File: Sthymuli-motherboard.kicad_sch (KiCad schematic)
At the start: 270 parts, among them J1 USB_C_Receptacle_USB2.0_16P, J2 Conn_01x09, J3 Conn_01x03, J4 Conn_01x06, Q1 Q_NMOS_Depletion_GSD, Q10 NX7002AK, Q11 NX7002AK, Q12 NX7002AK, Q13 NX7002AK, Q14 NX7002AK, Q15 NX7002AK, Q2 Q_NMOS_Depletion_GSD, Q3 Q_NMOS_Depletion_GSD, Q4 Q_NMOS_Depletion_GSD, Q5 Q_NMOS_Depletion_GSD, Q6 Q_NMOS_Depletion_GSD, Q7 PMOS, Q8 NX7002AK, Q9 NX7002AK, SW1 SW_Push, SW10 SW_Push, SW2 SW_Push, SW3 SW_Push, SW4 SW_Push, SW5 SW_Push, SW6 SW_Push, SW7 SW_Push, SW8 SW_Push, SW9 SW_Push, U1 ESP32-S3-WROOM-1, U10 74HC4051, U11 MCP6L01x-xOT, U12 74HC4051, U13 LSM6DS3, U14 LSM6DS3, U15 ITR9909, U16 ITR9909, U17 ITR9909, U18 ITR9909, U19 ITR9909, U2 AP2112K-3.3, U20 ITR9909, U21 ITR9909, U22 ITR9909, U3 BQ76905RGRR, U4 AP62300WU, U5 BQ25713, U6 AP62300WU, U7 MCP23017_SO, U8 AP22913CN4, U9 IRM-H6xxT

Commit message: progress on layout
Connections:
- net GND: no longer C80.2, C82.2, C83.2, R49.1
- net GNDA: now also C80.2, C82.2, C83.2, R49.1
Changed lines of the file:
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@@
 	)
 	(symbol
+		(lib_id "power:GNDA")
+		(at 360.68 88.9 0)
+		(unit 1)
+		(exclude_from_sim no)
+		(in_bom yes)
+		(on_board yes)
+		(dnp no)
+		(property "Reference" "#PWR082"
+			(at 360.68 95.25 0)
+			(effects
+				(font
+					(size 1.27 1.27)
+				)
+				(hide yes)
+			)
+		)
+		(property "Value" "GNDA"
+			(at 364.49 88.9 0)
+			(effects
+				(font
+					(size 1.27 1.27)
+				)
+			)
+		)
+		(property "Footprint" ""
+			(at 360.68 88.9 0)
+			(effects
+				(font
+					(size 1.27 1.27)
+				)
+				(hide yes)
+			)
+		)
+		(property "Datasheet" ""
+			(at 360.68 88.9 0)
+			(effects
+				(font
+					(size 1.27 1.27)
+				)
+				(hide yes)
+			)
+		)
+		(property "Description" "Power symbol creates a global label with name \"GNDA\" , analog ground"
+			(at 360.68 88.9 0)
+			(effects
+				(font
+					(size 1.27 1.27)
+				)
+				(hide yes)
+			)
+		)
+		(pin "1"
+		)
+		(instances
+			(project "Sthymuli-motherboard"
+				(path "/a56c3281-40b7-4048-95ca-500415dc80a4"
+					(reference "#PWR082")
+					(unit 1)
+				)
+			)
+		)
+	)
+	(symbol
 		(lib_id "Connector_Generic:Conn_01x03")
 		(at 231.14 374.65 0)
@@
 					(unit 1)
 				)
-			)
-		)
-	)
-	(symbol
-		(lib_id "power:GND")
-		(at 360.68 88.9 0)
-		(mirror y)
-		(unit 1)
-		(exclude_from_sim no)
-		(in_bom yes)
-		(on_board yes)
-		(dnp no)
-		(property "Reference" "#PWR082"
-			(at 360.68 95.25 0)
-			(effects
-				(font
-					(size 1.27 1.27)
-				)
-				(hide yes)
-			)
-		)
-		(property "Value" "GND"
-			(at 358.394 88.9 0)
-			(effects
-				(font
-					(size 1.27 1.27)
-				)
-			)
-		)
-		(property "Footprint" ""
-			(at 360.68 88.9 0)
-			(effects
-				(font
-					(size 1.27 1.27)
-				)
-				(hide yes)
-			)
-		)
-		(property "Datasheet" ""
-			(at 360.68 88.9 0)
-			(effects
-				(font
-					(size 1.27 1.27)
-				)
-				(hide yes)
-			)
-		)
-		(property "Description" "Power symbol creates a global label with name \"GND\" , ground"
-			(at 360.68 88.9 0)
-			(effects
-				(font
-					(size 1.27 1.27)
-				)
-				(hide yes)
-			)
-		)
-		(pin "1"
-		)
-		(instances
-			(project "Sthymuli-motherboard"
-				(path "/a56c3281-40b7-4048-95ca-500415dc80a4"
-					(reference "#PWR082")
-					(unit 1)
-				)

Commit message: starting from scratch the routing. autorouter was not good
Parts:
- removed BT1, BT2, BT3: Battery_Cell, sthymuli:Battery_Holder_18650_robop, symbol Device:Battery_Cell
- removed C10, C11, C12, C13, C14, C15, C16, C17, C18, C19, C20, C21, C22, C23, C24, C25, C77, C8, C9: 100nF, Capacitor_SMD:C_0402_1005Metric, symbol Device:C
- removed D10, D11, D12, D13, D14, D15, D16, D17, D18, D19, D20, D21, D22, D23, D24, D25, D8, D9: WS2812B, LED_SMD:LED_WS2812B_PLCC4_5.0x5.0mm_P3.2mm, symbol LED:WS2812B
- removed D26, D27, D28: D_Schottky, Diode_SMD:D_SOD-123F, symbol Device:D_Schottky
- removed F1, F2, F3: Fuse, Resistor_SMD:R_0805_2012Metric, symbol Device:Fuse
- removed Q10, Q11, Q12, Q13, Q14, Q15: NX7002AK, Package_TO_SOT_SMD:SOT-23, symbol Transistor_FET_Other:Q_NMOS_Depletion_GSD
- removed R52, R53, R54, R55, R56, R57: 3K3, Capacitor_SMD:C_0201_0603Metric, symbol Device:R
- removed R62, R63, R64, R65, R66, R67: 27R, Capacitor_SMD:C_0201_0603Metric, symbol Device:R
- removed SW10, SW5, SW6, SW7, SW8, SW9: SW_Push, sthymuli:XKB5858, symbol Switch:SW_Push
- removed U13: LSM6DS3, Package_LGA:LGA-14_3x2.5mm_P0.5mm_LayoutBorder3x4y, symbol Sensor_Motion:LSM6DS3
- removed U17, U18: ITR9909, sthymuli:ITR_9909_Horizontal, symbol kitprisme:ITR9909
- removed U19, U20, U21, U22: ITR9909, sthymuli:ITR_9909_Vertical, symbol kitprisme:ITR9909
- added J11, J12, J8: Conn_02x08_Counter_Clockwise, Connector_PinSocket_2.54mm:PinSocket_2x08_P2.54mm_Vertical_SMD, symbol Connector_Generic:Conn_02x08_Counter_Clockwise
- J2: footprint Connector_PinHeader_2.54mm:PinHeader_1x09_P2.54mm_Vertical -> Connector_PinSocket_2.54mm:PinSocket_1x09_P2.54mm_Vertical_SMD_Pin1Left
- J3: footprint Connector_PinHeader_2.54mm:PinHeader_1x03_P2.54mm_Vertical -> Connector_PinSocket_2.54mm:PinSocket_1x03_P2.54mm_Vertical_SMD_Pin1Left
- U3: footprint Package_DFN_QFN:Texas_RGP0020H_VQFN-20-1EP_4x4mm_P0.5mm_EP2.4x2.4mm -> BQ76905RGRR:IC_BQ76905RGRR
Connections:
- net +3V3: now also J11.2 (Pin_2), J12.2 (Pin_2), J8.2 (Pin_2)
- net +5V: now also J11.1 (Pin_1), J12.1 (Pin_1), J8.1 (Pin_1)
- net +BATT: now also J11.6 (Pin_6)
- net ACC_B_INT1: now also J12.16 (Pin_16)
- net GND: now also J1.SH (SHIELD), J11.3 (Pin_3), J12.3 (Pin_3), J8.3 (Pin_3); no longer J1.S1 (SHIELD)
- net SCL: now also J11.15 (Pin_15), J12.15 (Pin_15), J8.15 (Pin_15)
- net SDA: now also J11.14 (Pin_14), J12.14 (Pin_14), J8.14 (Pin_14)
- net EAST_BAT+: now reaches R3.1
- net EAST_BAT+: now also J12.7 (Pin_7), J8.6 (Pin_6)
- net at D7.2 (DOUT): now also J8.8 (Pin_8)
- net NORTH_BAT-: now reaches BT4.2 (-), D29.2 (A), R13.2, R14.2, R6.1
- net SOUTH_BAT+: now reaches R2.1
- net SOUTH_BAT+: now also J11.7 (Pin_7), J12.6 (Pin_6)
- net EAST_BAT-: now reaches D29.1 (K), F4.1, R4.1
- net EAST_BAT-: now also J8.7 (Pin_7)
- net INT_WS2812_DIN renamed WS2812_DIN
- net IR_REC_0 renamed NORTH_IR_REC_HORI
- net NORTH_IR_REC_HORI: now also U10.14 (A1); no longer U10.13 (A0)
- net IR_REC_1 renamed NORTH_IR_REC_VERT
- net NORTH_IR_REC_VERT: now also U10.13 (A0); no longer U10.14 (A1)
- net IR_REC_2 renamed EAST_IR_REC_VERT
- net EAST_IR_REC_VERT: now also J8.12 (Pin_12)
- net IR_REC_3 renamed EAST_IR_REC_HORI
- net EAST_IR_REC_HORI: now also J8.10 (Pin_10)
- net IR_REC_4 renamed SOUTH_IR_REC_VERT
- net SOUTH_IR_REC_VERT: now also J12.12 (Pin_12)
- net IR_REC_5 renamed SOUTH_IR_REC_HORI
- net SOUTH_IR_REC_HORI: now also J12.10 (Pin_10)
- net IR_REC_6 renamed WEST_IR_REC_VERT
- net WEST_IR_REC_VERT: now also J11.12 (Pin_12)
- net IR_REC_7 renamed WEST_IR_REC_HORI
- net WEST_IR_REC_HORI: now also J11.10 (Pin_10)
- net IR_TRA_0 renamed NORTH_IR_TRA_HORI
- net NORTH_IR_TRA_HORI: now also U12.14 (A1); no longer U12.13 (A0)
- net IR_TRA_1 renamed NORTH_IR_TRA_VERT
- net NORTH_IR_TRA_VERT: now also U12.13 (A0); no longer U12.14 (A1)
- net IR_TRA_2 renamed EAST_IR_TRA_VERT
- net EAST_IR_TRA_VERT: now also J8.13 (Pin_13)
- net IR_TRA_3 renamed EAST_IR_TRA_HORI
- net EAST_IR_TRA_HORI: now also J8.11 (Pin_11)
- net IR_TRA_4 renamed SOUTH_IR_TRA_VERT
- net SOUTH_IR_TRA_VERT: now also J12.13 (Pin_13)
- net IR_TRA_5 renamed SOUTH_IR_TRA_HORI
- net SOUTH_IR_TRA_HORI: now also J12.11 (Pin_11)
- net IR_TRA_6 renamed WEST_IR_TRA_VERT
- net WEST_IR_TRA_VERT: now also J11.13 (Pin_13)
- net IR_TRA_7 renamed WEST_IR_TRA_HORI
- net WEST_IR_TRA_HORI: now also J11.11 (Pin_11)
- net btn_EAST_DOWN renamed SOUTH_btn_B
- net SOUTH_btn_B: now also J12.5 (Pin_5)
- net btn_EAST_UP renamed SOUTH_btn_A
- net SOUTH_btn_A: now also J12.4 (Pin_4)
- net btn_NORTH_DOWN renamed NORTH_btn_A
- net NORTH_btn_A: now also U7.1 (GPB0); no longer U7.2 (GPB1)
- net btn_NORTH_UP renamed NORTH_btn_B
- net NORTH_btn_B: now also U7.2 (GPB1); no longer U7.1 (GPB0)
- net btn_SOUTH_DOWN renamed EAST_btn_B
- net EAST_btn_B: now also J8.5 (Pin_5)
- net btn_SOUTH_UP renamed EAST_btn_A
- net EAST_btn_A: now also J8.4 (Pin_4)
- net btn_WEST_DOWN renamed WEST_btn_B
- net WEST_btn_B: now also J11.5 (Pin_5)
- net btn_WEST_UP renamed WEST_btn_A
- net WEST_btn_A: now also J11.4 (Pin_4)
- new net: J11.8 (Pin_8), J12.9 (Pin_9)
- new net: J12.8 (Pin_8), J8.9 (Pin_9)
- no-connect marks 22 -> 23
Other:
- note added: "Buttons"
- note added: "EAST"
- note added: "LED 1-7"
- note added: "LED 14-19"
- note added: "LED 20-25"
- note added: "LED 8-13"
- note added: "NORTH (this board)"
- note added: "SOUTH"
- note added: "WEST"
- note added: "cardinalboard EAST"
- note added: "cardinalboard SOUTH"
- note added: "cardinalboard WEST"
- note added: "daughterboard (center)"
- note added: "for max current draw, check regulators (~3A)"
- note removed: "1101011b = 0x5B"
- note removed: "Buttons/switch"
- note removed: "duplicated to infer rotation / translation around real donut center. if not wanted, leave unpopulated"
- note removed: "for max current draw, check regulators"
- note removed: "we use MCP23017 internal pull-ups"
- moved on the sheet: BT4, C1, C2, C3, C4, C5, C6, C7, C76, C78, C79, C80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

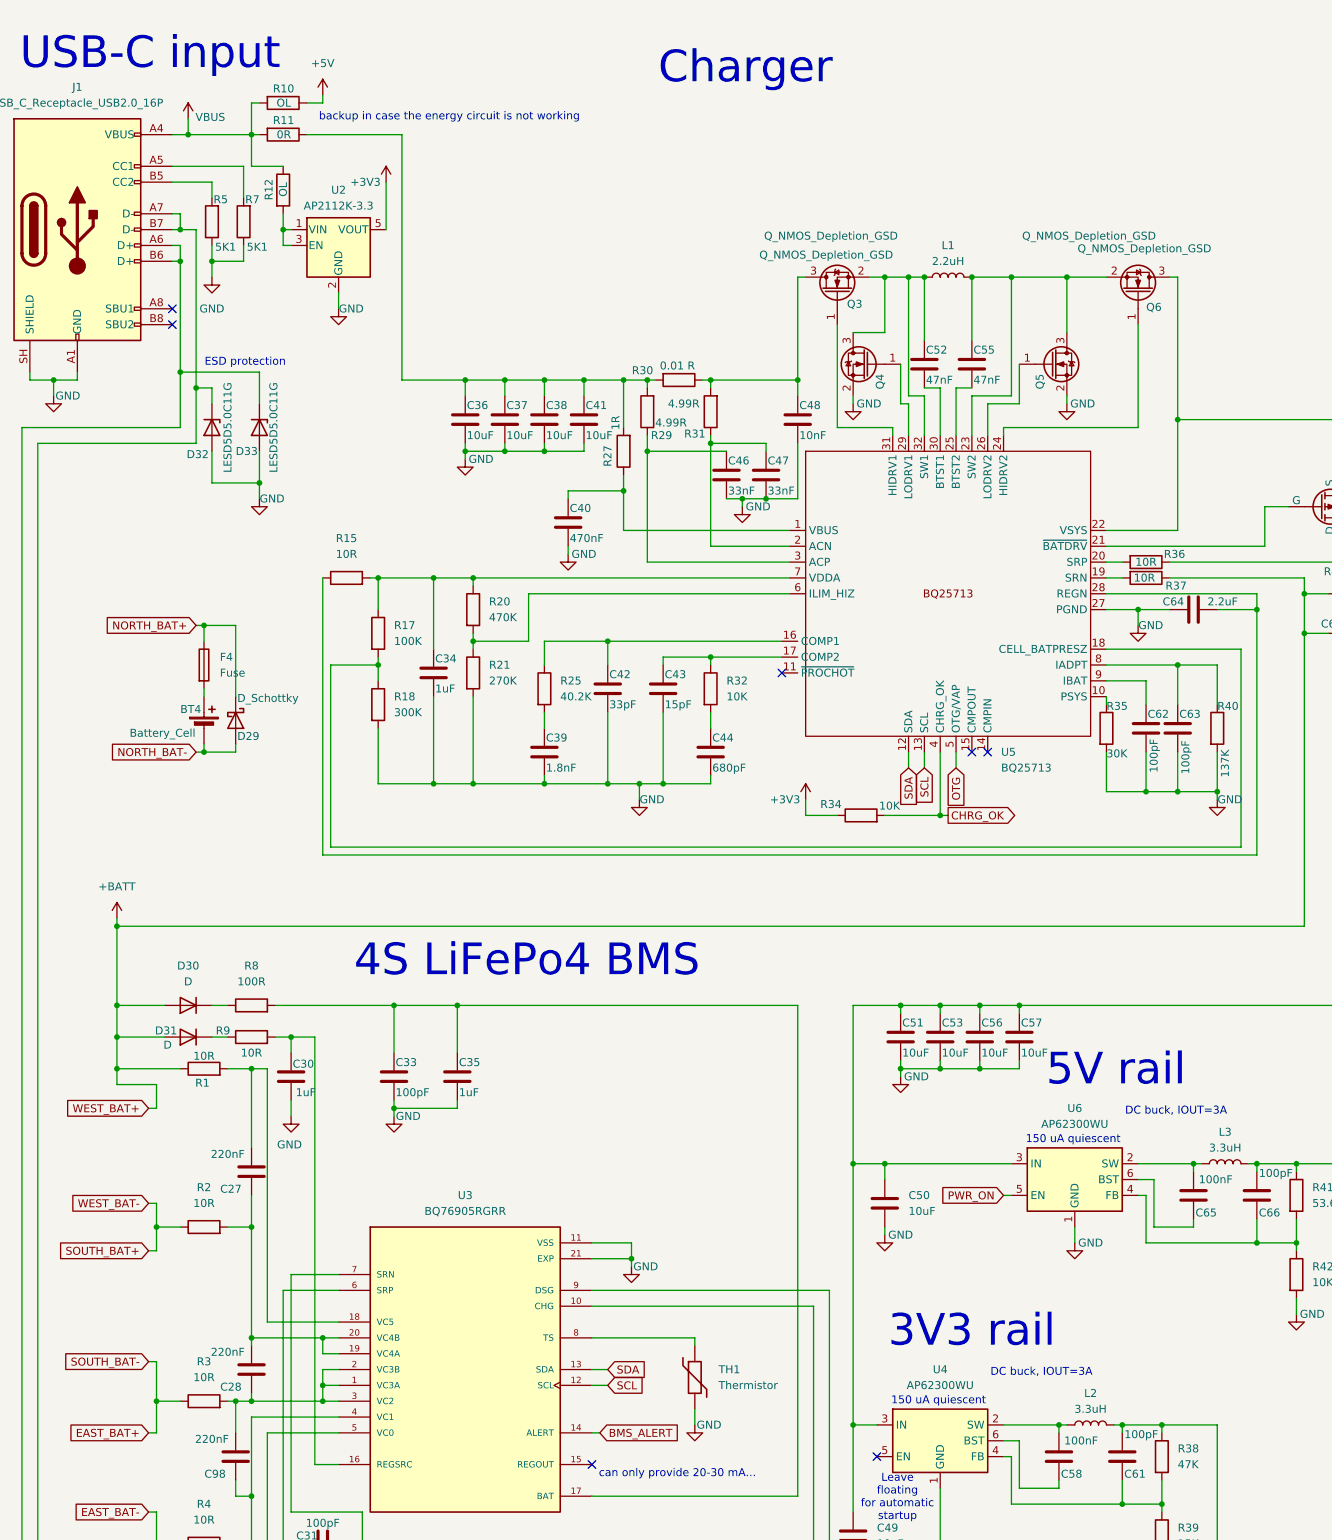
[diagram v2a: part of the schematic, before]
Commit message: 280 left to route, power mostly done
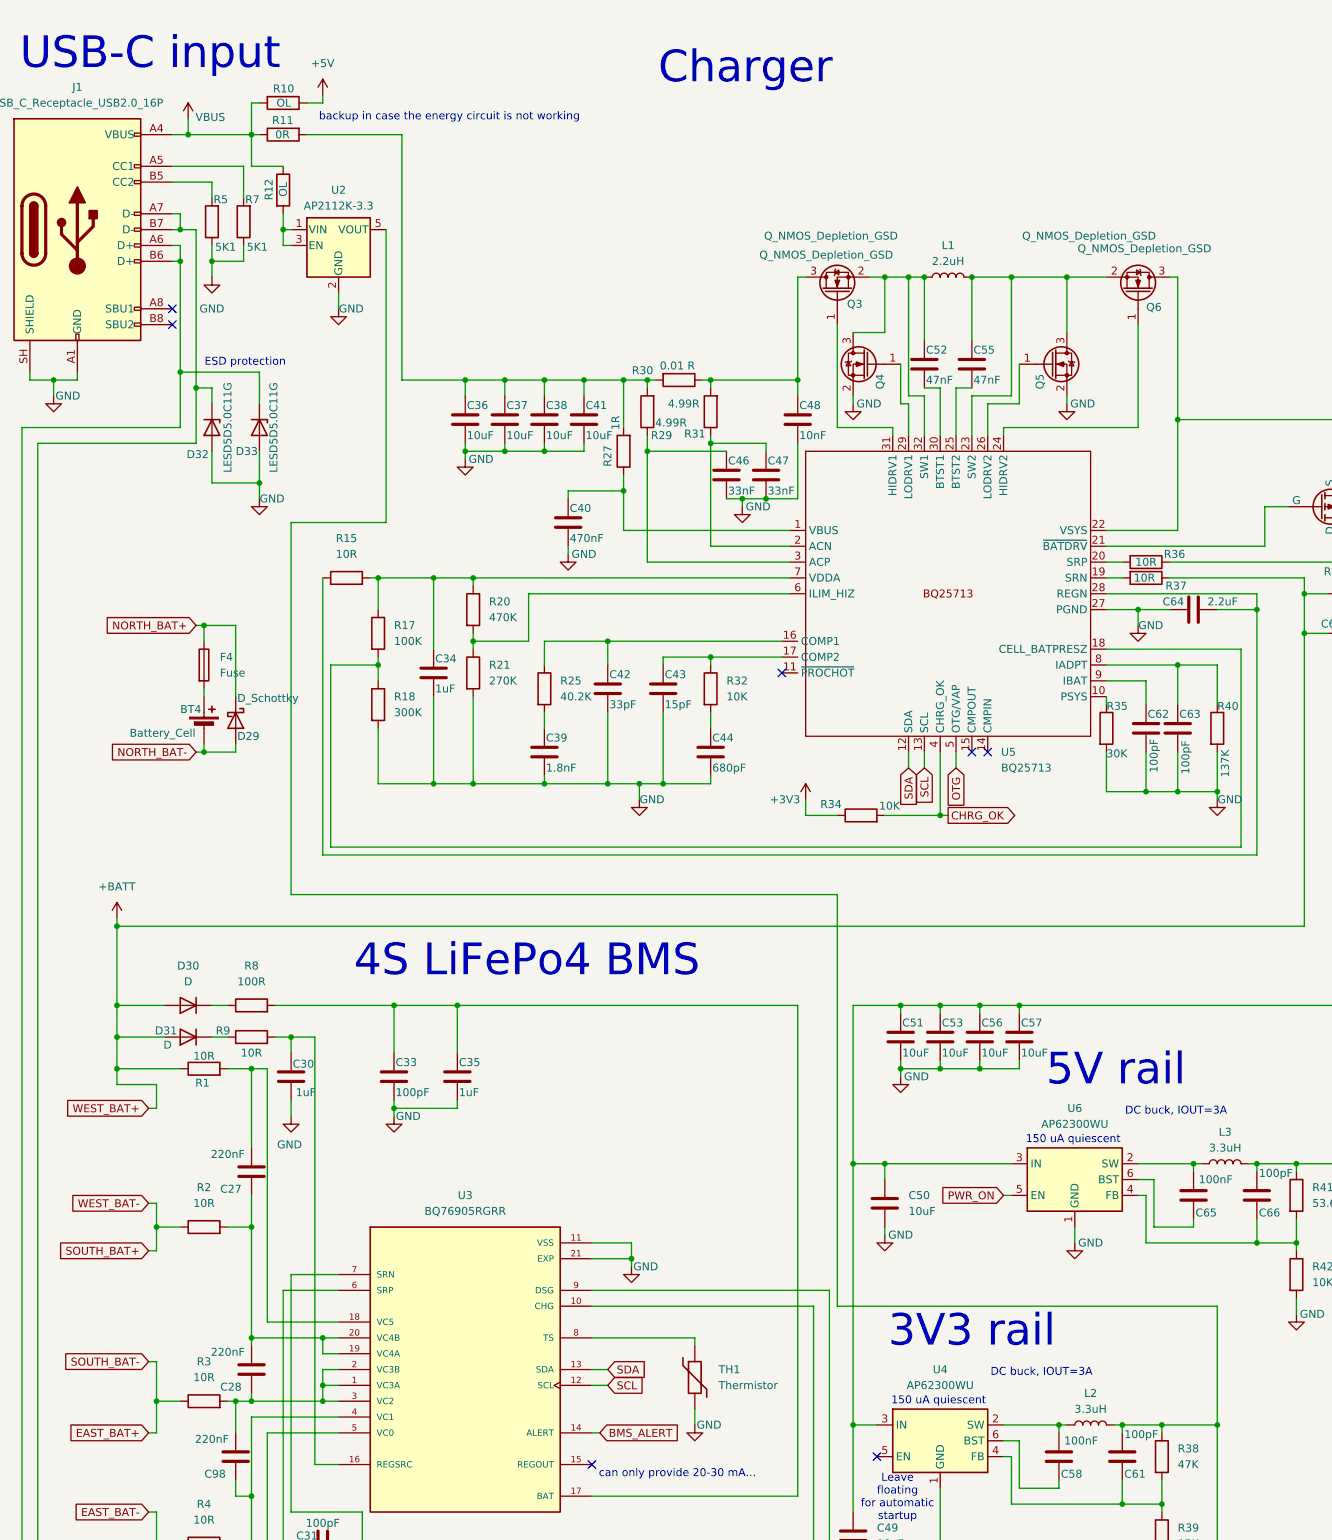
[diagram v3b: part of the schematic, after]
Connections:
- net +3V3: no longer U2.5 (VOUT)
- net VBUS: now also R11.1; no longer R11.2
- net at C59.2, C60.2, C61.2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: now also U2.5 (VOUT)
- net at C36.1, C37.1, C38.1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: now also R11.2; no longer R11.1
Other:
- moved on the sheet: R11
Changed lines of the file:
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@@
 	)
 	(junction
+		(at 210.82 257.81)
+		(diameter 0)
+		(color 0 0 0 0)
+	)
+	(junction
 		(at 172.72 190.5)
 		(diameter 0)
@@
 	(wire
 		(pts
-			(xy 77.47 58.42) (xy 77.47 66.04)
-		)
-		(stroke
-			(width 0)
-			(type default)
-		)
-	)
-	(wire
-		(pts
 			(xy 40.64 207.01) (xy 40.64 203.2)
 		)
@@
 	(wire
 		(pts
+			(xy 77.47 113.03) (xy 62.23 113.03)
+		)
+		(stroke
+			(width 0)
+			(type default)
+		)
+	)
+	(wire
+		(pts
 			(xy 240.03 119.38) (xy 240.03 124.46)
 		)
@@
 	(wire
 		(pts
+			(xy 62.23 113.03) (xy 62.23 172.72)
+		)
+		(stroke
+			(width 0)
+			(type default)
+		)
+	)
+	(wire
+		(pts
 			(xy 368.3 195.58) (xy 370.84 195.58)
 		)
@@
 	(wire
 		(pts
+			(xy 77.47 66.04) (xy 77.47 113.03)
+		)
+		(stroke
+			(width 0)
+			(type default)
+		)
+	)
+	(wire
+		(pts
 			(xy 102.87 135.89) (xy 102.87 132.08)
 		)
@@
 	(wire
 		(pts
+			(xy 149.86 238.76) (xy 210.82 238.76)
+		)
+		(stroke
+			(width 0)
+			(type default)
+		)
+	)
+	(wire
+		(pts
 			(xy 393.7 87.63) (xy 396.24 87.63)
 		)
@@
 	(wire
 		(pts
+			(xy 210.82 238.76) (xy 210.82 257.81)
+		)
+		(stroke
+			(width 0)
+			(type default)
+		)
+	)
+	(wire
+		(pts
 			(xy 40.64 222.25) (xy 40.64 226.06)
 		)
@@
 	(wire
 		(pts
+			(xy 62.23 172.72) (xy 149.86 172.72)
+		)
+		(stroke
+			(width 0)
+			(type default)
+		)
+	)
+	(wire
+		(pts
 			(xy 411.48 142.24) (xy 403.86 142.24)
 		)
@@
 	(wire
 		(pts
+			(xy 149.86 172.72) (xy 149.86 238.76)
+		)
+		(stroke
+			(width 0)
+			(type default)
+		)
+	)
+	(wire
+		(pts
 			(xy 130.81 382.27) (xy 130.81 384.81)
 		)
@@
 		(lib_id "power:+BATT")
 		(at 34.29 176.53 0)
+		(mirror y)
 		(unit 1)
 		(body_style 1)
@@
 		(in_pos_files yes)
 		(dnp no)
-		(fields_autoplaced yes)
 		(property "Reference" "#PWR03"
 			(at 34.29 180.34 0)
@@
 	(symbol
 		(lib_id "Device:R")
-		(at 60.96 50.8 270)
+		(at 60.96 50.8 90)
+		(mirror x)
 		(unit 1)
 		(body_style 1)
@@
 		(dnp no)
 		(property "Reference" "R11"
-			(at 62.738 48.514 90)
+			(at 59.182 48.514 90)
 			(show_name no)
 			(do_not_autoplace no)
@@
 		)
 		(property "Value" "0R"
-			(at 62.23 50.8 90)
+			(at 59.69 50.8 90)
 			(show_name no)
 			(do_not_autoplace no)
@@
 					(unit 1)
 				)
-			)
-		)
-	)
-	(symbol
-		(lib_id "power:+3V3")
-		(at 77.47 58.42 0)
-		(unit 1)
-		(body_style 1)
-		(exclude_from_sim no)
-		(in_bom yes)
-		(on_board yes)
-		(in_pos_files yes)
-		(dnp no)
-		(property "Reference" "#PWR012"
-			(at 77.47 62.23 0)
-			(hide yes)
-			(show_name no)
-			(do_not_autoplace no)
-			(effects
-				(font
-					(size 1.27 1.27)
-				)
-			)
-		)
-		(property "Value" "+3V3"
-			(at 74.168 58.42 0)
-			(show_name no)
-			(do_not_autoplace no)
-			(effects
-				(font
-					(size 1.27 1.27)
-				)
-			)
-		)
-		(property "Footprint" ""
-			(at 77.47 58.42 0)
-			(hide yes)
-			(show_name no)
-			(do_not_autoplace no)
-			(effects
-				(font
-					(size 1.27 1.27)
-				)
-			)
-		)
-		(property "Datasheet" ""
-			(at 77.47 58.42 0)
-			(hide yes)
-			(show_name no)
-			(do_not_autoplace no)
-			(effects
-				(font
-					(size 1.27 1.27)
-				)
-			)
-		)
-		(property "Description" "Power symbol creates a global label with name \"+3V3\""
-			(at 77.47 58.42 0)
-			(hide yes)
-			(show_name no)
-			(do_not_autoplace no)
-			(effects
-				(font
-					(size 1.27 1.27)
-				)
-			)
-		)
-		(pin "1"
-		)
-		(instances
-			(project "Sthymuli-motherboard"
-				(path "/a56c3281-40b7-4048-95ca-500415dc80a4"
-					(reference "#PWR012")
-					(unit 1)
-				)

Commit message: done routing
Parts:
- U16: footprint sthymuli:ITR_9909_Horizontal -> sthymuli:ITR_9909_Vertical
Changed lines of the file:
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@@
 			)
 		)
-		(property "Footprint" "sthymuli:ITR_9909_Horizontal"
+		(property "Footprint" "sthymuli:ITR_9909_Vertical"
 			(at 289.56 261.62 0)
 			(hide yes)

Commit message: cleaning board
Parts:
- U1: footprint RF_Module:ESP32-S3-WROOM-1 -> sthymuli:ESP32-S3-WROOM-1
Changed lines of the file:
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@@
 			)
 		)
-		(property "Footprint" "RF_Module:ESP32-S3-WROOM-1"
+		(property "Footprint" "sthymuli:ESP32-S3-WROOM-1"
 			(at 52.07 370.84 0)
 			(hide yes)
